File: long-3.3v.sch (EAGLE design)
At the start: 47 parts, among them J1 CON_HEADER_1X06-SMD-RIGHT-ANG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, Q1 BSS84, U2 MCP73831, U3 MCP9808T-E/MC, X1 Micro USB, X2 CRYSTAL, X3 CRYSTALS-NOGND-IQXC-25

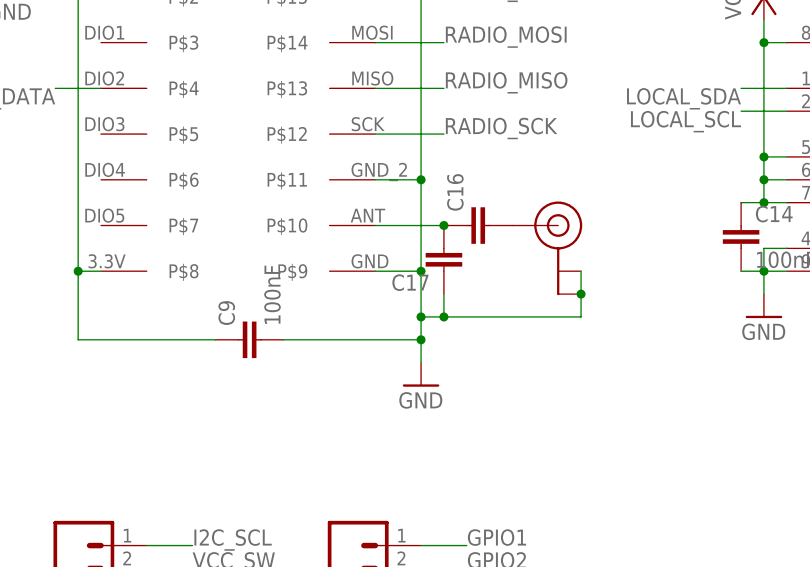
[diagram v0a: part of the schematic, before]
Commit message: Fixed Silks
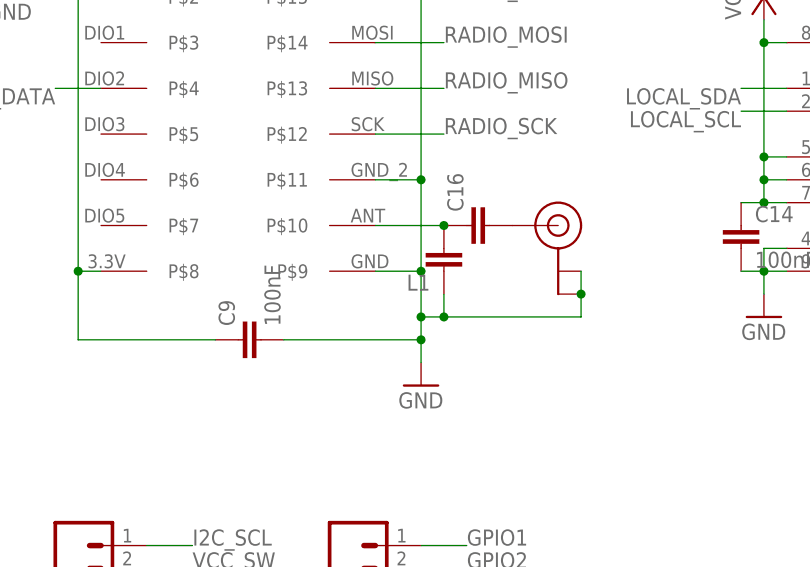
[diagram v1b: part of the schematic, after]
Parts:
- renumbered C17 to L1
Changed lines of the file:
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@@
 <?xml version="1.0" encoding="utf-8"?>
 <!DOCTYPE eagle SYSTEM "eagle.dtd">
-<eagle version="7.2.0">
+<eagle version="7.3.0">
 <drawing>
 <settings>
@@
 <part name="GND6" library="supply1" deviceset="GND" device=""/>
 <part name="C16" library="rcl" deviceset="C-EU" device="C0402"/>
-<part name="C17" library="rcl" deviceset="C-EU" device="C0402"/>
+<part name="L1" library="rcl" deviceset="C-EU" device="C0402"/>
 <part name="GND8" library="supply1" deviceset="GND" device=""/>
 <part name="D1" library="SparkFun" deviceset="LED" device="0603" value="POWER"/>
@@
 <instance part="GND6" gate="1" x="185.42" y="40.64"/>
 <instance part="C16" gate="G$1" x="248.92" y="106.68" rot="R90"/>
-<instance part="C17" gate="G$1" x="246.38" y="101.6" rot="R180"/>
+<instance part="L1" gate="G$1" x="246.38" y="101.6" rot="R180"/>
 <instance part="GND8" gate="1" x="198.12" y="132.08"/>
 <instance part="D1" gate="G$1" x="0" y="63.5"/>
@@
 <junction x="261.62" y="99.06"/>
 <junction x="243.84" y="96.52"/>
-<pinref part="C17" gate="G$1" pin="1"/>
+<pinref part="L1" gate="G$1" pin="1"/>
 <wire x1="246.38" y1="96.52" x2="243.84" y2="96.52" width="0.1524" layer="91"/>
 <wire x1="246.38" y1="99.06" x2="246.38" y2="96.52" width="0.1524" layer="91"/>
@@
 <segment>
 <pinref part="C16" gate="G$1" pin="1"/>
-<pinref part="C17" gate="G$1" pin="2"/>
+<pinref part="L1" gate="G$1" pin="2"/>
 <pinref part="U$3" gate="G$1" pin="P$10"/>
 <wire x1="238.76" y1="106.68" x2="246.38" y2="106.68" width="0.1524" layer="91"/>

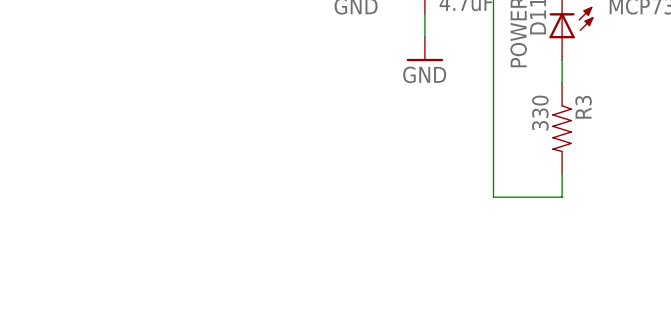
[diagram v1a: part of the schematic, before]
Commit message: Added EARS Logo
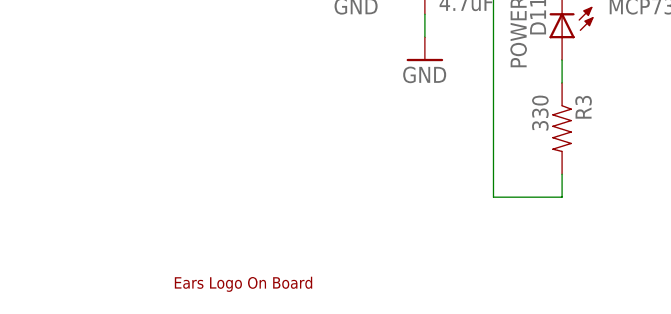
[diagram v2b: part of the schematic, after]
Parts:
- added U$2: EARS-LOGO, earsLogo:EARS-LOGO
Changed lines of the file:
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@@
 <?xml version="1.0" encoding="utf-8"?>
 <!DOCTYPE eagle SYSTEM "eagle.dtd">
-<eagle version="7.3.0">
+<eagle version="7.2.0">
 <drawing>
 <settings>
@@
 <part name="R11" library="SparkFun" deviceset="RESISTOR" device="0402-RES" value="330"/>
 <part name="GND10" library="supply1" deviceset="GND" device=""/>
+<part name="U$2" library="earsLogo" deviceset="EARS-LOGO" device=""/>
 </parts>
 <sheets>
@@
 <instance part="R11" gate="G$1" x="0" y="73.66" rot="R90"/>
 <instance part="GND10" gate="1" x="0" y="55.88"/>
+<instance part="U$2" gate="G$1" x="0" y="0"/>
 </instances>
 <busses>
